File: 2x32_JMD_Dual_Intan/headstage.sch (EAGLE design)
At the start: 23 parts, among them U1 ADXL335

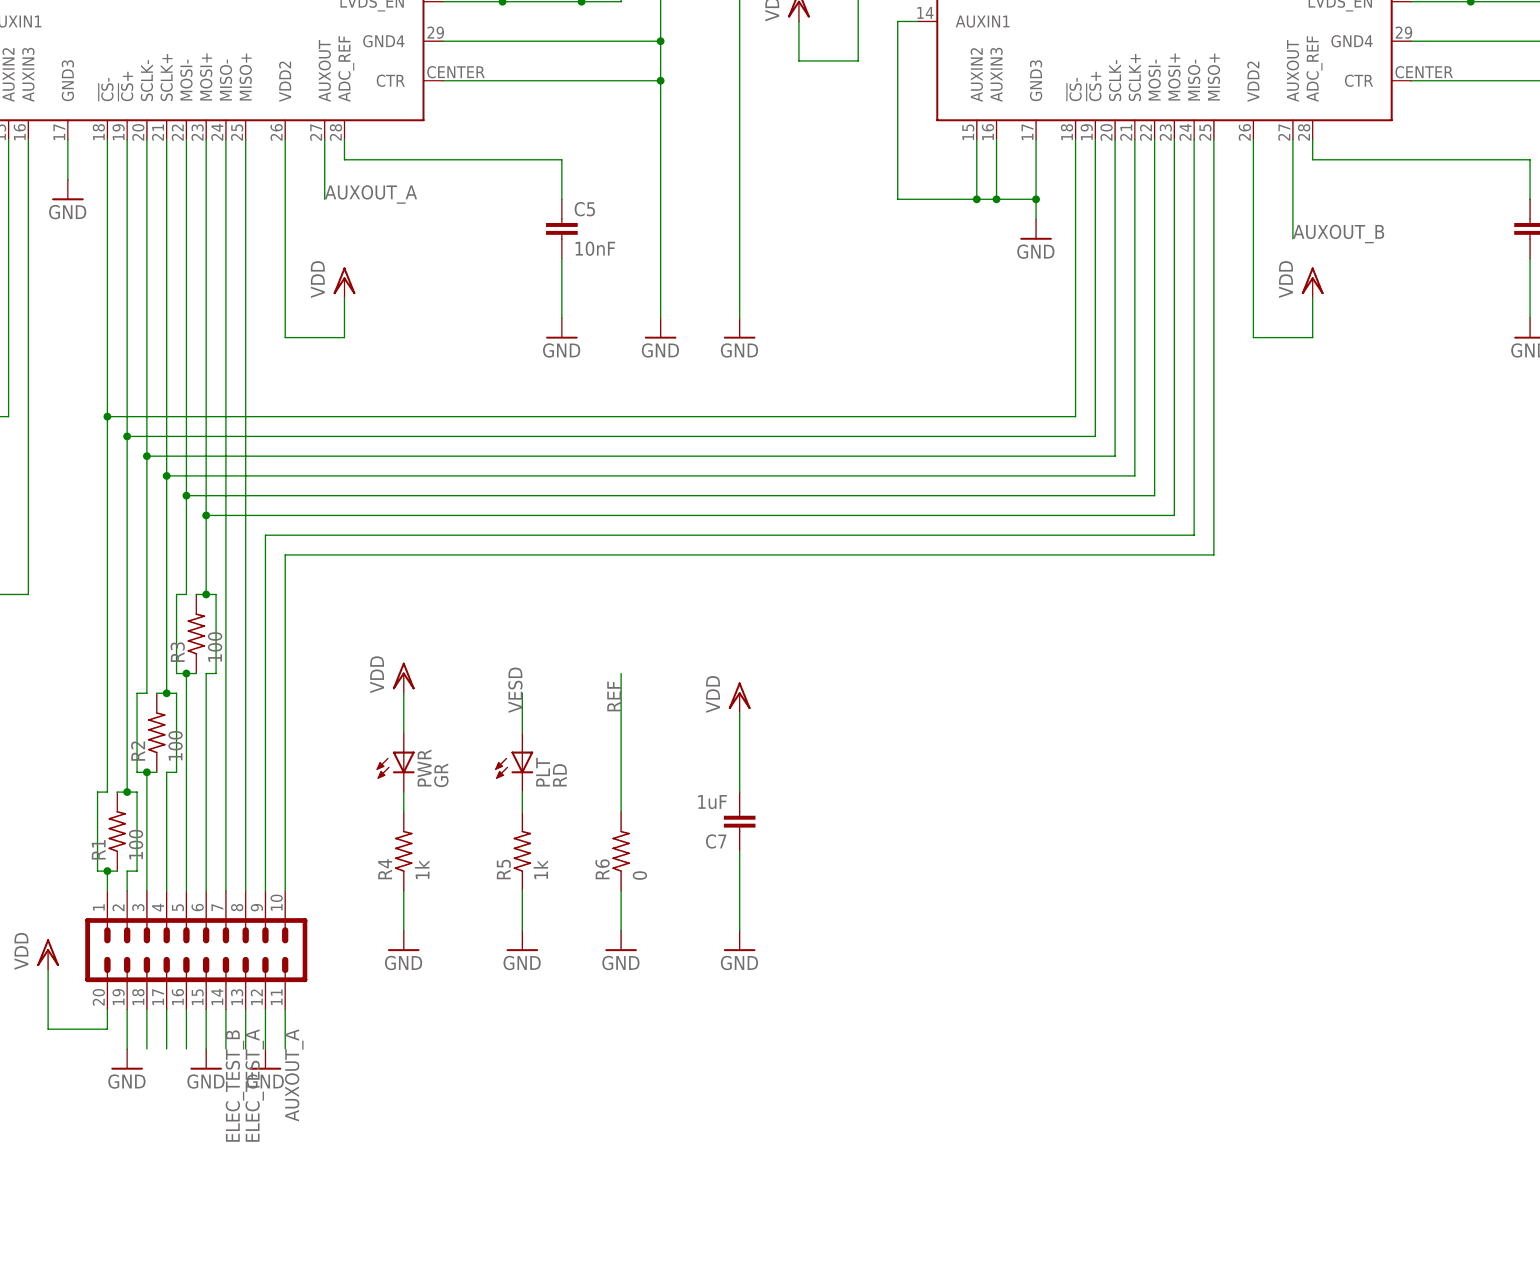
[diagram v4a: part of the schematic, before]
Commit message: Completed rev. 0 of the 64 channel JMD headstage, sent off for fabrication.
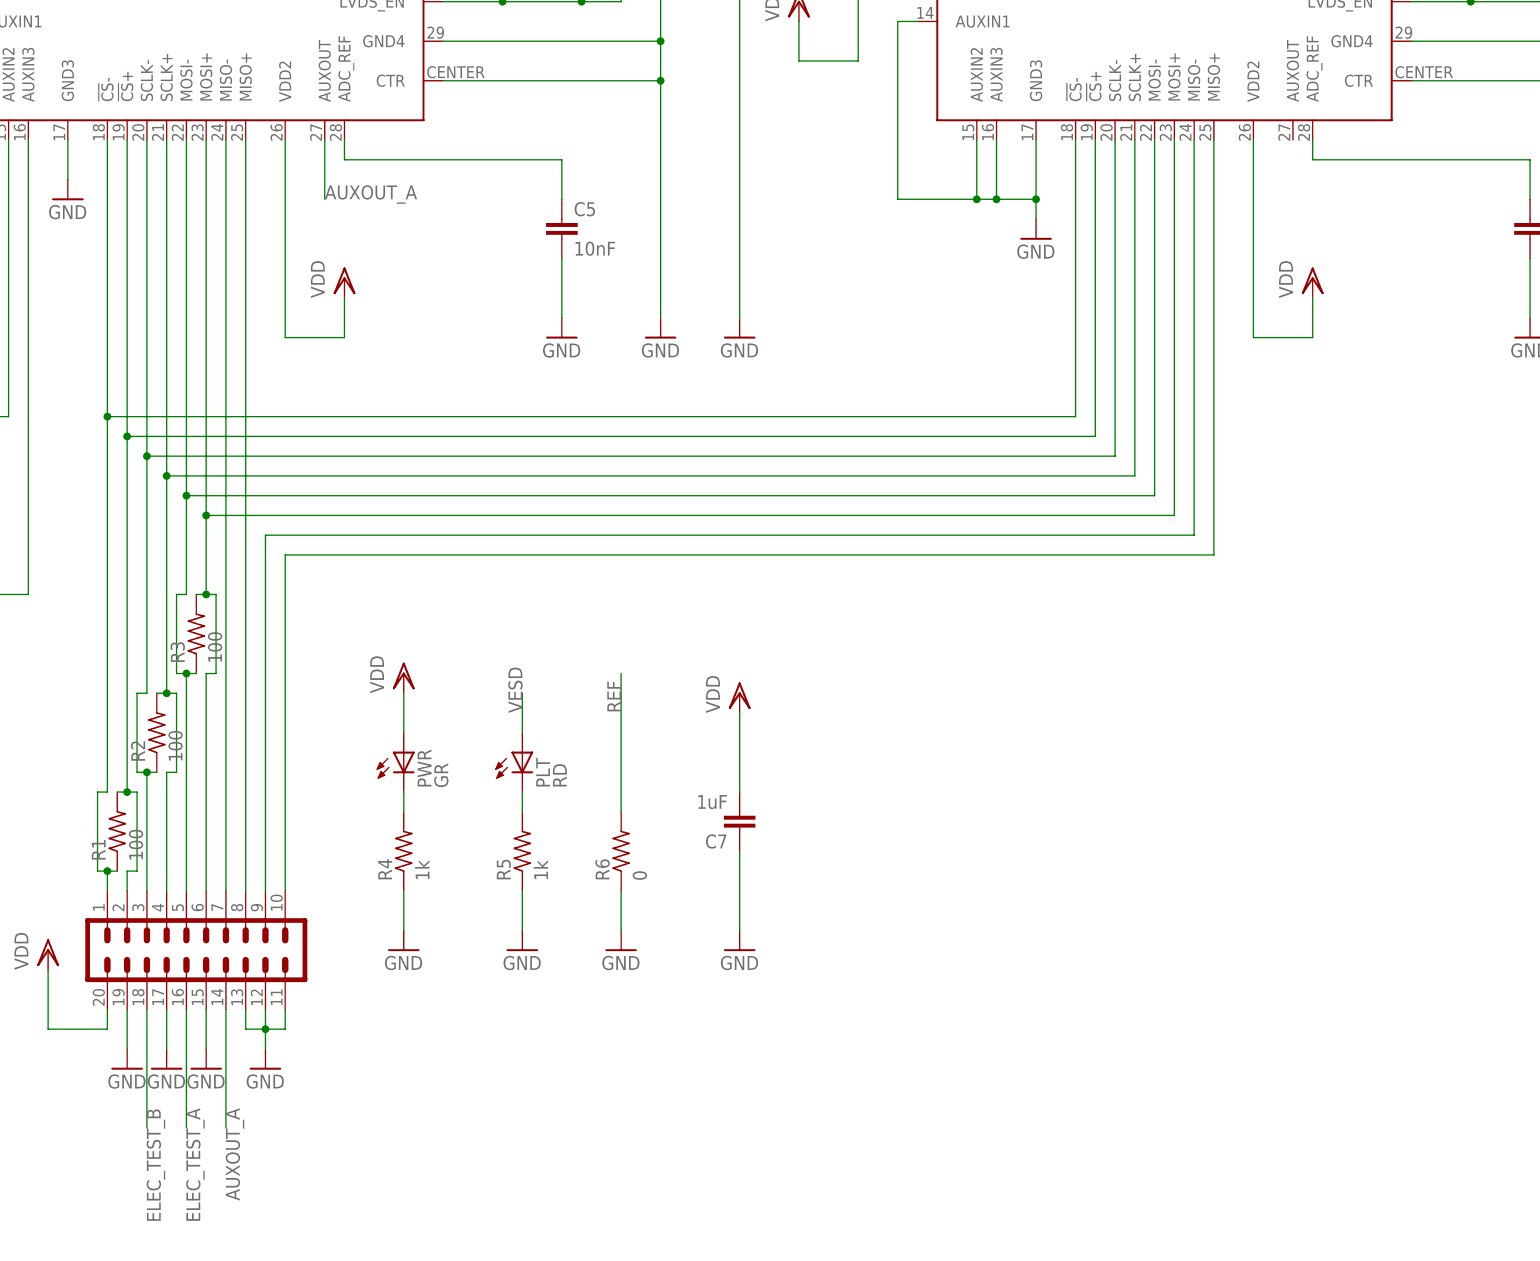
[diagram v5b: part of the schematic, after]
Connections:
- removed net AUXOUT_B: RHD_B.AUXOUT
- removed net N$10: OUT.16
- removed net N$8: OUT.18
- removed net N$9: OUT.17
- net AUXOUT_A: now also OUT.14; no longer OUT.11
- net ELEC_TEST_A: now also OUT.16; no longer OUT.13
- net ELEC_TEST_B: now also OUT.18; no longer OUT.14
- net GND: now also OUT.11, OUT.13, OUT.17
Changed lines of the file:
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@@
 <part name="VDD2" library="headstage" deviceset="VDD" device=""/>
 <part name="GND7" library="headstage" deviceset="GND" device=""/>
+<part name="GND8" library="headstage" deviceset="GND" device=""/>
 </parts>
 <sheets>
@@
 <instance part="VDD2" gate="G$1" x="203.2" y="88.9"/>
 <instance part="GND7" gate="1" x="203.2" y="55.88"/>
+<instance part="GND8" gate="1" x="129.54" y="40.64"/>
 </instances>
 <busses>
@@
 <segment>
 <pinref part="OUT" gate="G$1" pin="12"/>
-<wire x1="142.24" y1="48.26" x2="142.24" y2="43.18" width="0.1524" layer="91"/>
+<wire x1="142.24" y1="48.26" x2="142.24" y2="45.72" width="0.1524" layer="91"/>
 <pinref part="GND4" gate="1" pin="GND"/>
+<pinref part="OUT" gate="G$1" pin="13"/>
+<wire x1="142.24" y1="45.72" x2="142.24" y2="43.18" width="0.1524" layer="91"/>
+<wire x1="139.7" y1="48.26" x2="139.7" y2="45.72" width="0.1524" layer="91"/>
+<wire x1="139.7" y1="45.72" x2="142.24" y2="45.72" width="0.1524" layer="91"/>
+<junction x="142.24" y="45.72"/>
+<pinref part="OUT" gate="G$1" pin="11"/>
+<wire x1="144.78" y1="48.26" x2="144.78" y2="45.72" width="0.1524" layer="91"/>
+<wire x1="144.78" y1="45.72" x2="142.24" y2="45.72" width="0.1524" layer="91"/>
 </segment>
 <segment>
@@
 <pinref part="C7" gate="C" pin="1"/>
 <wire x1="203.2" y1="68.58" x2="203.2" y2="58.42" width="0.1524" layer="91"/>
+</segment>
+<segment>
+<pinref part="OUT" gate="G$1" pin="17"/>
+<wire x1="129.54" y1="48.26" x2="129.54" y2="43.18" width="0.1524" layer="91"/>
+<pinref part="GND8" gate="1" pin="GND"/>
 </segment>
 </net>
@@
 </segment>
 <segment>
-<pinref part="OUT" gate="G$1" pin="11"/>
-<wire x1="144.78" y1="48.26" x2="144.78" y2="43.18" width="0.1524" layer="91"/>
-<label x="144.78" y="45.72" size="1.778" layer="95" rot="R270"/>
+<pinref part="OUT" gate="G$1" pin="14"/>
+<wire x1="137.16" y1="48.26" x2="137.16" y2="33.02" width="0.1524" layer="91"/>
+<label x="137.16" y="35.56" size="1.778" layer="95" rot="R270"/>
 </segment>
 </net>
@@
 </segment>
 </net>
-<net name="AUXOUT_B" class="0">
-<segment>
-<pinref part="RHD_B" gate="A" pin="AUXOUT"/>
-<wire x1="274.32" y1="160.02" x2="274.32" y2="147.32" width="0.1524" layer="91"/>
-<label x="274.32" y="147.32" size="1.778" layer="95"/>
-</segment>
-</net>
 <net name="ELEC_TEST_A" class="0">
 <segment>
@@
 </segment>
 <segment>
-<pinref part="OUT" gate="G$1" pin="13"/>
-<wire x1="139.7" y1="48.26" x2="139.7" y2="43.18" width="0.1524" layer="91"/>
-<label x="139.7" y="45.72" size="1.778" layer="95" rot="R270"/>
+<pinref part="OUT" gate="G$1" pin="16"/>
+<wire x1="132.08" y1="48.26" x2="132.08" y2="33.02" width="0.1524" layer="91"/>
+<label x="132.08" y="35.56" size="1.778" layer="95" rot="R270"/>
 </segment>
 </net>
@@
 </segment>
 <segment>
-<pinref part="OUT" gate="G$1" pin="14"/>
-<wire x1="137.16" y1="48.26" x2="137.16" y2="43.18" width="0.1524" layer="91"/>
-<label x="137.16" y="45.72" size="1.778" layer="95" rot="R270"/>
+<pinref part="OUT" gate="G$1" pin="18"/>
+<wire x1="127" y1="48.26" x2="127" y2="33.02" width="0.1524" layer="91"/>
+<label x="127" y="35.56" size="1.778" layer="95" rot="R270"/>
 </segment>
 </net>
@@
 </segment>
 </net>
-<net name="N$8" class="0">
-<segment>
-<pinref part="OUT" gate="G$1" pin="18"/>
-<wire x1="127" y1="48.26" x2="127" y2="43.18" width="0.1524" layer="91"/>
-</segment>
-</net>
-<net name="N$9" class="0">
-<segment>
-<pinref part="OUT" gate="G$1" pin="17"/>
-<wire x1="129.54" y1="48.26" x2="129.54" y2="43.18" width="0.1524" layer="91"/>
-</segment>
-</net>
-<net name="N$10" class="0">
-<segment>
-<pinref part="OUT" gate="G$1" pin="16"/>
-<wire x1="132.08" y1="48.26" x2="132.08" y2="43.18" width="0.1524" layer="91"/>
-</segment>
-</net>
 <net name="LEDOUT2" class="0">
 <segment>
@@
 </sheet>
 </sheets>
+<errors>
+</errors>
 </schematic>
 </drawing>

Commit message: Halfway through a dual SPI interface board, with integrated head tracking, for the JMD headstage.
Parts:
- OUT: device headstage:PINHD-2X10_JMD -> headstage:PINHD-2X10_JMD-RA
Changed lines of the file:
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@@
 <part name="R6" library="headstage" deviceset="R" device="_0402" value="0"/>
 <part name="GND2" library="headstage" deviceset="GND" device=""/>
-<part name="OUT" library="headstage" deviceset="PINHD-2X10" device="_JMD" value="JMD"/>
+<part name="OUT" library="headstage" deviceset="PINHD-2X10" device="_JMD-RA" value="JMD"/>
 <part name="VDD1" library="headstage" deviceset="VDD" device=""/>
 <part name="GND3" library="headstage" deviceset="GND" device=""/>
